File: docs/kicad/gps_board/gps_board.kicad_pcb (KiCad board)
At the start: 2 copper layers, 72.4 x 67.3 mm, 22 parts, among them J1 NMEA2000, J2 SEATALK, J3 BUCK_PWR, J4 12V_TEST, J5 5V_TEST, J6 SN65HVD230, J7 NEO6M, J8 EN_SEATALK, J9 EN_NMEA2000, M1 BUCK01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

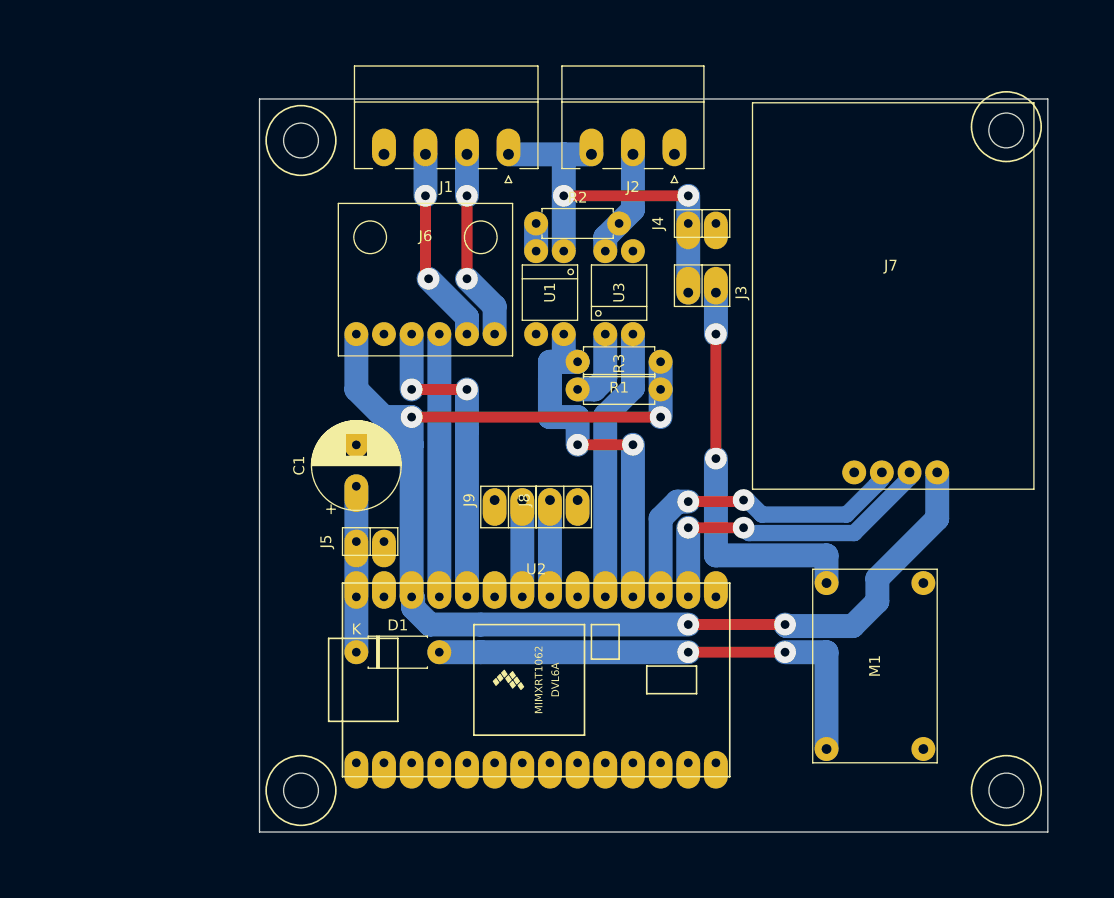
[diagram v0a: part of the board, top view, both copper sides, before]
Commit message: redesigned teensyGPS board (removed jumpers; needs EEPROM) before rotating for flatcam
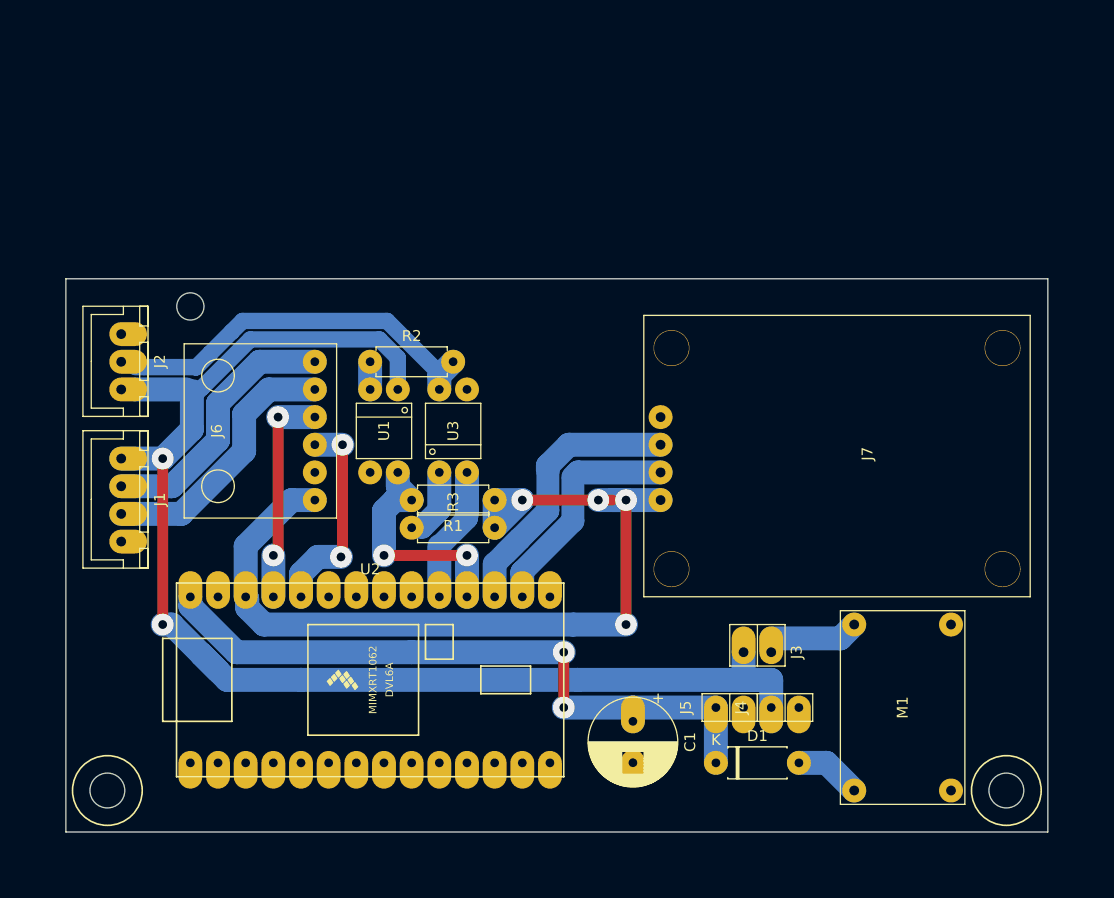
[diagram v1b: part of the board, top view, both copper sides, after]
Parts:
- removed J8: EN_SEATALK, 0_my_footprints2:pinHeader1x2
- removed J9: EN_NMEA2000, 0_my_footprints2:pinHeader1x2
- removed the REF** at (80.0, 12.7)
- removed the REF** at (15.2, 73.7)
- removed the REF** at (15.2, 14.0)
- added REF**: myMountingHole_2.5mm, 0_my_footprints:myMountingHole_2.5mm, F.Cu at (5.08, 29.2)
- added REF**: myMountingHole_3.2mm_M3, 0_my_footprints:myMountingHole_3.2mm_M3, F.Cu at (-2.54, 73.7)
- J1: footprint 0_my_footprints:myPheonix4x3.81_right -> 0_my_footprints2:JST4
- J2: footprint 0_my_footprints:myPheonix3x3.81_right -> 0_my_footprints2:JST3
- moved J2 53.4 mm to (-1.27, 31.8), turned to 270 degrees
- moved J1 45.2 mm to (-1.27, 43.2), turned to 270 degrees
- moved J4 45.1 mm to (58.4, 66.0)
- moved J5 36.4 mm to (53.3, 66.0)
- moved D1 34.5 mm to (53.3, 71.1)
- moved J3 33.4 mm to (58.4, 61.0)
- moved C1 33.3 mm to (45.7, 67.3), turned to 270 degrees
- moved R3 19.8 mm to (25.4, 49.5)
- moved R2 19.8 mm to (21.6, 34.3)
- moved U1 19.8 mm to (22.9, 40.6)
- moved U3 19.8 mm to (29.2, 40.6)
- moved R1 19.8 mm to (33.0, 47.0)
- moved J7 18.5 mm to (48.3, 39.4), turned to 270 degrees
- moved U2 15.2 mm to (5.08, 71.1)
- moved J6 13.5 mm to (16.5, 40.6), turned to 90 degrees
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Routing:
- net +12V: track 36.8 -> 124.3 mm
- net +5V: track 15.2 -> 62.3 mm, vias 0 -> 2
- net Net-(D1-Pad2): track 44.4 -> 6.13 mm, vias 2 -> 0
- net +3V3: track 118.7 -> 85.2 mm
- net Net-(J3-Pad1): track 36.8 -> 8.15 mm, vias 2 -> 0
- net ST1: track 9.94 -> 36.3 mm
- net RX4: track 38.9 -> 21.5 mm
- net TX4: track 25.2 -> 12.5 mm
- net CRX: track 29.2 -> 19.3 mm
- net EN_SEATALK: track 8.89 -> 0.00 mm
- net EN_NMEA200: track 8.89 -> 0.00 mm
- net CANL: track 17.6 -> 24.5 mm, vias 2 -> 0
- net CANH: track 18.1 -> 24.5 mm, vias 2 -> 0
- net TX3: track 29.5 -> 25.0 mm, vias 2 -> 0
- net CTX: track 24.1 -> 20.1 mm, vias 0 -> 2
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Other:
- board size 72.4 x 67.3 mm -> 90.2 x 50.8 mm

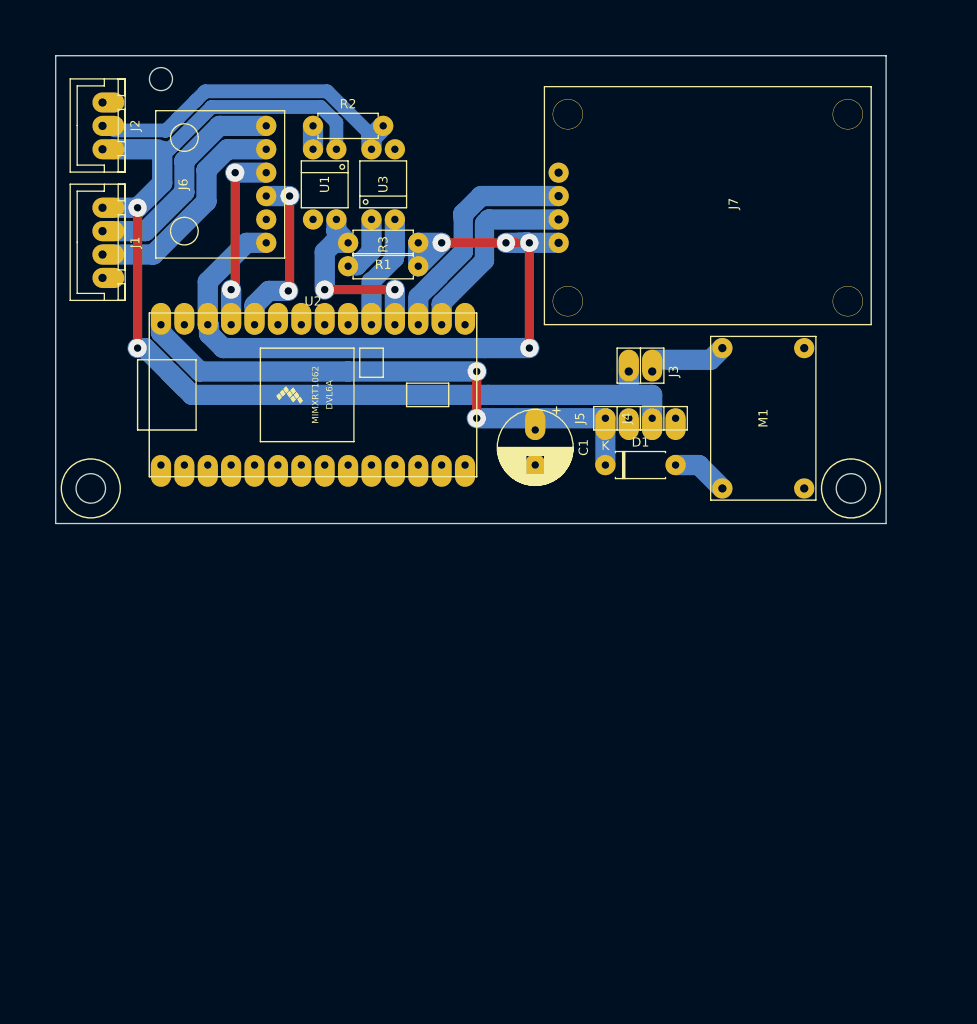
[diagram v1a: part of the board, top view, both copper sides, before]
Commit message: did flatcam stuff and milled teensyGPS PCB
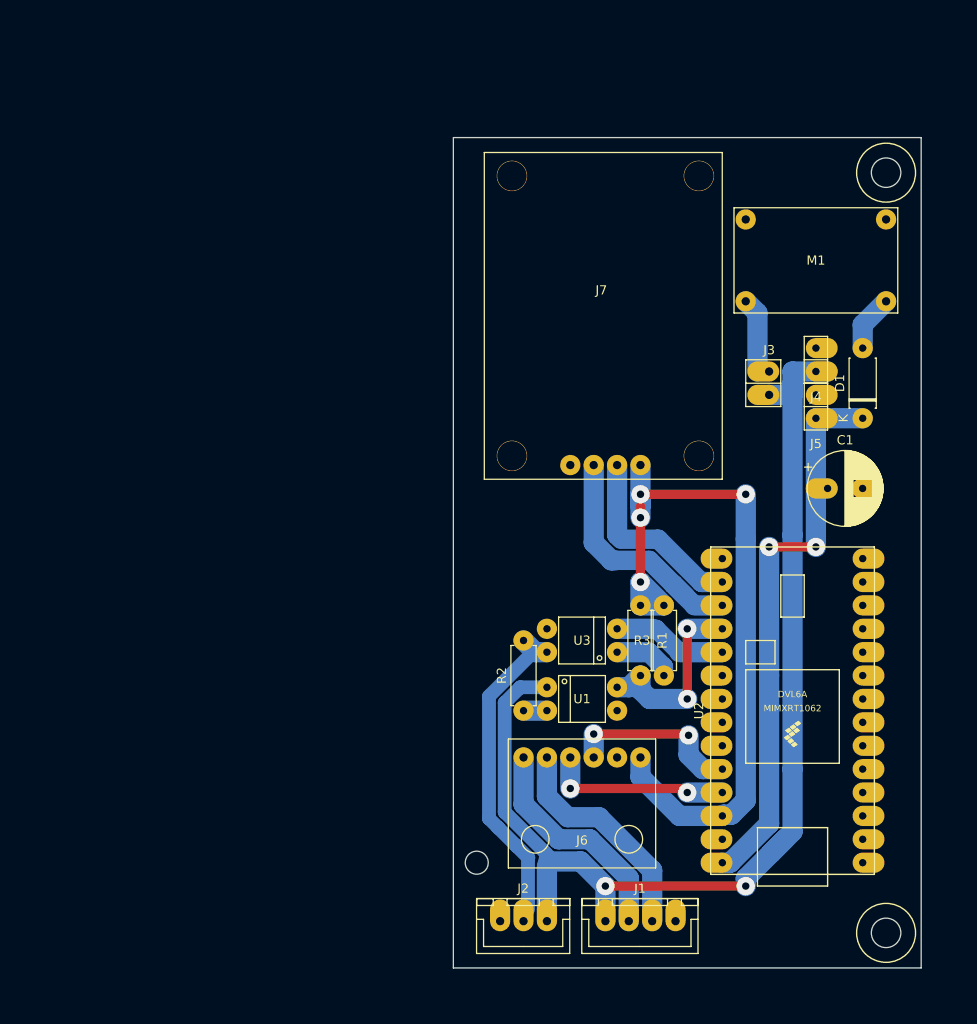
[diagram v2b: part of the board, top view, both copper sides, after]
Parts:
- removed the REF** at (80.0, 73.7)
- removed the REF** at (-2.54, 73.7)
- added REF**: myMountingHole_3.2mm_M3, 0_my_footprints:myMountingHole_3.2mm_M3, F.Cu at (83.8, 39.4)
- added REF**: myMountingHole_3.2mm_M3, 0_my_footprints:myMountingHole_3.2mm_M3, F.Cu at (83.8, 121.9)
- moved J2 98.8 mm to (41.9, 120.7), turned to 0 degrees
- moved J1 94.8 mm to (53.3, 120.7), turned to 0 degrees
- moved REF** 91.7 mm to (39.4, 114.3), turned to 90 degrees
- moved U2 87.6 mm to (81.3, 114.3), turned to 90 degrees
- moved J6 71.1 mm to (50.8, 102.9), turned to 180 degrees
- moved R2 67.5 mm to (44.5, 97.8), turned to 90 degrees
- moved U1 62.5 mm to (50.8, 96.5), turned to 0 degrees
- moved R3 56.1 mm to (59.7, 94.0), turned to 90 degrees
- moved U3 54.0 mm to (50.8, 90.2), turned to 180 degrees
- moved R1 46.2 mm to (57.1, 86.4), turned to 270 degrees
- moved C1 32.4 mm to (77.5, 73.7), turned to 0 degrees
- moved J7 31.8 mm to (49.5, 71.1), turned to 0 degrees
- moved D1 28.4 mm to (81.3, 66.0), turned to 90 degrees
- moved J5 22.9 mm to (76.2, 66.0), turned to 180 degrees
- moved M1 19.1 mm to (73.7, 44.5), turned to 0 degrees
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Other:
- board size 90.2 x 50.8 mm -> 50.8 x 90.2 mm

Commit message: show resistor values switch jst jumpers
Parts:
- moved J1 7.62 mm to (61.0, 120.7), turned to 180 degrees
- moved J2 5.08 mm to (47.0, 120.7), turned to 180 degrees
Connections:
- net EN_NMEA200 renamed Net-(U2-Pad22)
- net EN_SEATALK renamed Net-(U2-Pad21)
- J1 pad 1: +12V -> GND
- J1 pad 2: CANL -> CANH
- J1 pad 3: CANH -> CANL
- J1 pad 4: GND -> +12V
- J2 pad 1: GND -> +12V
- J2 pad 3: +12V -> GND
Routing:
- net +3V3: track 85.2 -> 83.9 mm
